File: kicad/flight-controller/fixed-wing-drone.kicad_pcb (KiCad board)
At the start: 4 copper layers, 91 x 61.5 mm, 81 parts, among them J1 1, J10 UWB SPI, J11 Inter ESP UART, J13 USB-C, J14 GPS/Compass, J15 Airspeed I2C, J16 8, J19 ESC2, J2 2, J20 FC UBEC Input, J22 ESC1, J3 3, J4 4, J5 5, J6 6, J7 RC Conn, J8 LIDAR I2C, J9 7, M2 MountingHole_2.2mm_M2, Q1 reverse polarity protection, Q2 reverse polarity protection, SW1 TS-1088, SW2 TS-1088, U1 ESP32-S3-WROOM-1, U2 Primary IMU, U3 Backup IMU, U4 XC6220B331PR-G, U6 AP2112K-3.3, U7 Barometer

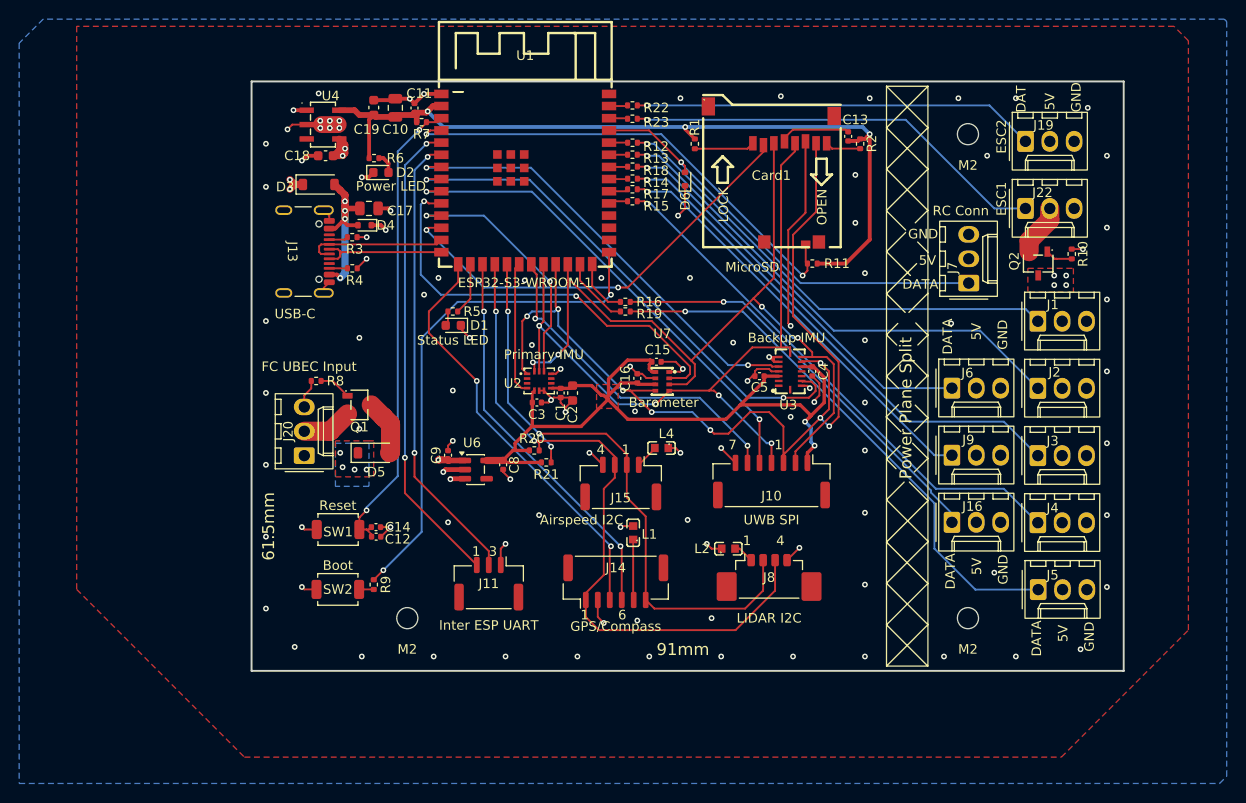
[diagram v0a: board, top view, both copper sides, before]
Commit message: removed basestation code and v3.1 of fc pcb
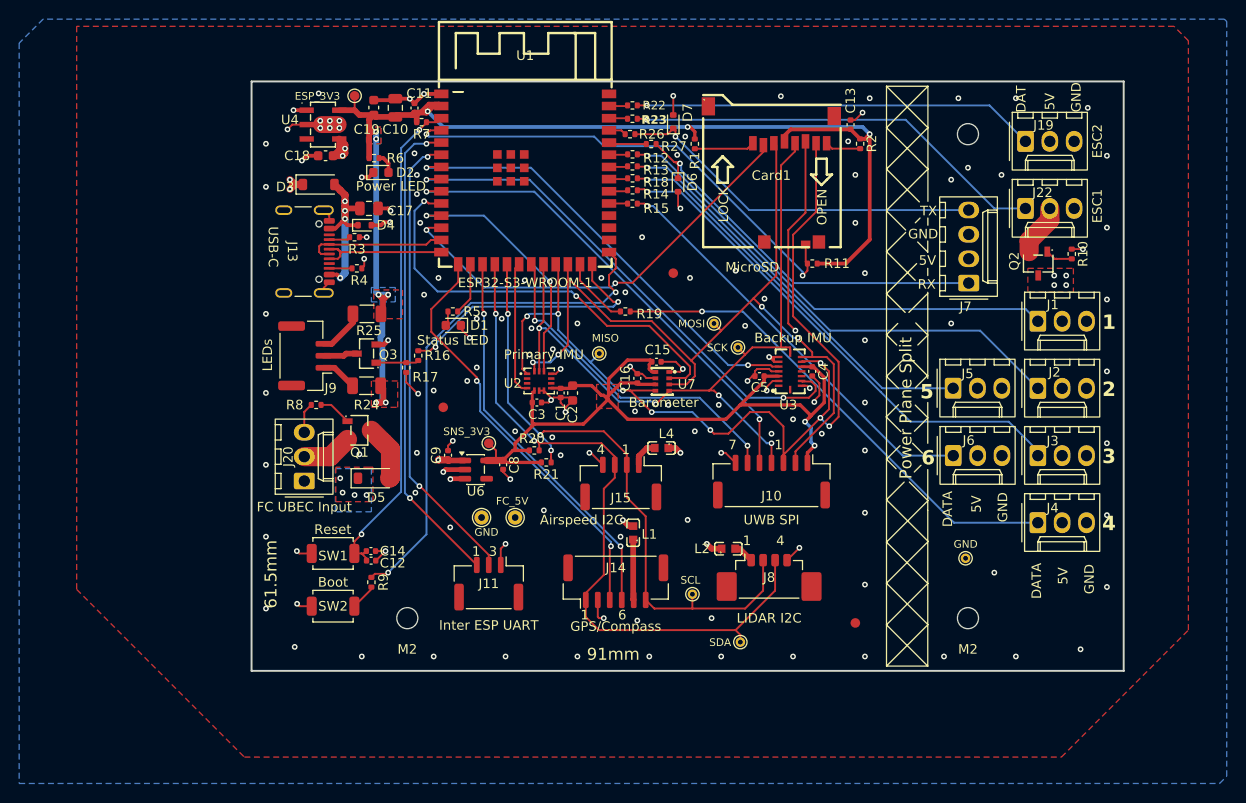
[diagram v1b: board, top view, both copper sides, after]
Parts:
- removed J16: 8, Connector_Molex:Molex_KK-254_AE-6410-03A_1x03_P2.54mm_Vertical
- added D7: ESD5Z5.0T1G, Diode_SMD:D_SOD-523, F.Cu at (142.2, 66.5)
- added Q3: AO3400A, easyeda2kicad:SOT-23-3_L2.9-W1.3-P1.90-LS2.4-BR, F.Cu at (110.2, 90.6)
- added R24: 33R, Resistor_SMD:R_1206_3216Metric, F.Cu at (110.2, 94.0)
- added R25: 33R, Resistor_SMD:R_1206_3216Metric, F.Cu at (110.3, 86.5)
- added R26: 330R, Resistor_SMD:R_0402_1005Metric, F.Cu at (137.7, 67.8)
- added R27: 330R, Resistor_SMD:R_0402_1005Metric, F.Cu at (139.9, 68.8)
- added REF**: Fiducial_1mm_Mask2mm, Fiducial:Fiducial_1mm_Mask2mm, F.Cu at (161.2, 118.8)
- added REF**: Fiducial_1mm_Mask2mm, Fiducial:Fiducial_1mm_Mask2mm, F.Cu at (142.2, 82.2)
- added REF**: Fiducial_1mm_Mask2mm, Fiducial:Fiducial_1mm_Mask2mm, F.Cu at (118.2, 96.2)
- added TP1: MOSI, TestPoint:TestPoint_THTPad_D1.0mm_Drill0.5mm, F.Cu at (146.5, 87.5)
- added TP10: GND, TestPoint:TestPoint_THTPad_D1.0mm_Drill0.5mm, F.Cu at (172.8, 112.0)
- added TP2: MISO, TestPoint:TestPoint_THTPad_D1.0mm_Drill0.5mm, F.Cu at (134.5, 90.6)
- added TP3: SCK, TestPoint:TestPoint_THTPad_D1.0mm_Drill0.5mm, F.Cu at (149.0, 90.0)
- added TP4: GND, TestPoint:TestPoint_THTPad_D1.5mm_Drill0.7mm, F.Cu at (122.2, 107.8)
- added TP5: SDA, TestPoint:TestPoint_THTPad_D1.0mm_Drill0.5mm, F.Cu at (149.2, 120.8)
- added TP6: SCL, TestPoint:TestPoint_THTPad_D1.0mm_Drill0.5mm, F.Cu at (144.2, 115.8)
- added TP7: ESP_3V3, TestPoint:TestPoint_Pad_D1.0mm, F.Cu at (109.0, 63.8)
- added TP8: SENSOR_3V3, TestPoint:TestPoint_Pad_D1.0mm, F.Cu at (123.0, 100.0)
- added TP9: FC_5V, TestPoint:TestPoint_THTPad_D1.5mm_Drill0.7mm, F.Cu at (125.8, 107.8)
- J7: footprint Connector_Molex:Molex_KK-254_AE-6410-03A_1x03_P2.54mm_Vertical -> Connector_Molex:Molex_KK-254_AE-6410-04A_1x04_P2.54mm_Vertical
- J9: value 7 -> Conn_01x03_Pin; footprint Connector_Molex:Molex_KK-254_AE-6410-03A_1x03_P2.54mm_Vertical -> Connector_JST:JST_GH_BM03B-GHS-TBT_1x03-1MP_P1.25mm_Vertical
- R16: value 330R -> 220R
- R17: value 330R -> 100K
- moved J9 68.3 mm to (103.8, 90.9), turned to 90 degrees
- moved R17 30.0 mm to (114.4, 92.1), turned to -90 degrees
- moved J5 22.8 mm to (171.5, 94.3)
- moved R16 22.3 mm to (115.6, 90.9), turned to -90 degrees
- moved J6 7.04 mm to (171.5, 101.3)
- moved D5 2.65 mm to (111.0, 103.7)
- moved Q1 2.65 mm to (109.5, 98.7)
- moved J20 2.65 mm to (103.8, 103.9)
- moved C12 2.55 mm to (110.7, 112.2)
- moved C14 2.55 mm to (110.7, 111.2)
- moved SW1 2.55 mm to (106.8, 111.5)
- moved R8 2.50 mm to (105.0, 96.0)
- moved SW2 1.82 mm to (106.8, 117.0)
- moved C13 1.26 mm to (160.8, 66.8), turned to -90 degrees
- moved R12 1.21 mm to (138.0, 69.9)
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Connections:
- net /SERVO_OUT4 renamed /SERVO_OUT_6
- net /SERVO_OUT5 renamed /SERVO_OUT_4
- net /SERVO_OUT8 renamed /LED_TOGGLE
- C13 pad 1: /ESP_3V3 -> GND
- C13 pad 2: Net-(Card1-VDD) -> /ESP_3V3
- Card1 pad 4: Net-(Card1-VDD) -> /ESP_3V3
- D4 pad 1: GND -> Net-(D3-A)
- D4 pad 2: Net-(D3-A) -> GND
- D6 pad 1: GND -> /actuator_io/RC_SBUS_TVS
- D6 pad 2: /RC_SBUS -> GND
- J7 pad 1: /RC_SBUS -> /actuator_io/RC_SBUS_TVS
- J9 pad 1: Net-(J9-Pin_1) -> /aux/IRLED_FEED_1
- J9 pad 2: /actuator_io/esc_io/SERVO_5V -> /aux/IRLED_SW
- J9 pad 3: GND -> /aux/IRLED_FEED_2
- R12 pad 1: /SERVO_OUT1 -> /SERVO_OUT_1
- R13 pad 1: /SERVO_OUT2 -> /SERVO_OUT_2
- R14 pad 1: /SERVO_OUT3 -> /SERVO_OUT_3
- R15 pad 2: Net-(J4-Pin_1) -> Net-(J6-Pin_1)
- R16 pad 2: Net-(J16-Pin_1) -> Net-(Q3-G)
- R17 pad 1: /SERVO_OUT7 -> Net-(Q3-G)
- R17 pad 2: Net-(J9-Pin_1) -> GND
- R18 pad 1: /SERVO_OUT6 -> /SERVO_OUT_5
- R18 pad 2: Net-(J6-Pin_1) -> Net-(J5-Pin_1)
- R19 pad 2: Net-(J5-Pin_1) -> Net-(J4-Pin_1)
- U1 pad 32: /SERVO_OUT7 -> /SERVO_OUT_3
- U1 pad 33: /SERVO_OUT3 -> /SERVO_OUT_5
- U1 pad 34: /SERVO_OUT6 -> /SERVO_OUT_2
- U1 pad 35: /SERVO_OUT2 -> /SERVO_OUT_1
- U1 pad 36: /SERVO_OUT1 -> /RC_SBUS
- U1 pad 37: /RC_SBUS -> /RC_TX
- U3 pad 2: unconnected-(U3-NC-Pad2) -> GND
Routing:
- net /ESP_3V3: track 86.2 -> 136.2 mm, vias 3 -> 9
- net Net-(J9-Pin_1): track 44.3 -> 0.00 mm, vias 1 -> 0
- net Net-(J16-Pin_1): track 43.9 -> 0.00 mm, vias 1 -> 0
- net /RC_SBUS: track 45.5 -> 3.95 mm, vias 1 -> 0
- net /actuator_io/RC_SBUS_TVS: track 0.00 -> 40.7 mm, vias 0 -> 1
- net Net-(D7-A1): track 0.00 -> 39.0 mm, vias 0 -> 1
- net /LED_TOGGLE: track 5.93 -> 28.6 mm, vias 0 -> 2
- net Net-(J5-Pin_1): track 57.4 -> 42.0 mm
- net GND: track 102.2 -> 110.5 mm, vias 99 -> 133
- net Net-(Card1-VDD): track 7.44 -> 0.00 mm
- net /aux/IRLED_FEED_2: track 0.00 -> 4.89 mm
- net Net-(Q3-G): track 0.00 -> 4.17 mm
- net Net-(J4-Pin_1): track 55.7 -> 51.7 mm
- net /aux/IRLED_FEED_1: track 0.00 -> 3.79 mm
- net /aux/IRLED_SW: track 0.00 -> 3.57 mm
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- added copper zone on B.Cu, net /ESP_3V3
- added copper zone on F.Cu, net /ESP_3V3
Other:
- board text added: "1"
- board text added: "2"
- board text added: "3"
- board text added: "4"
- board text added: "5"
- board text added: "6"
- board text added: "ESP_3V3"
- board text added: "FC_5V"
- board text added: "LEDs"
- board text added: "MISO"
- board text added: "MOSI"
- board text added: "RX"
- board text added: "SCK"
- board text added: "SCL"
- board text added: "SDA"
- board text added: "SNS_3V3"
- board text added: "TX"

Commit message: pcb progress
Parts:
- added D8: ESD5Z5.0T1G, Diode_SMD:D_SOD-523, F.Cu at (112.8, 81.5)
- added D9: ESD5Z5.0T1G, Diode_SMD:D_SOD-523, F.Cu at (113.5, 78.5)
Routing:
- net GND: track 110.5 -> 114.1 mm, vias 133 -> 136
- net /esp32s3/DATA-: track 14.8 -> 15.6 mm
- net /esp32s3/DATA+: track 14.9 -> 15.6 mm

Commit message: Kicad FC v3.1 complete, Mission Controller and UWB boards v1 complete, firmware v2 complete!
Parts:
- removed D8, D9: ESD5Z5.0T1G, Diode_SMD:D_SOD-523
- removed Q1, Q2: reverse polarity protection, easyeda2kicad:SOT-23-3_L2.9-W1.6-P1.90-LS2.8-BR
- removed R10, R8: 100K, Resistor_SMD:R_0402_1005Metric
- added C20: 22uF, Capacitor_SMD:C_0805_2012Metric, F.Cu at (178.1, 81.8)
- added L3: Ferrite Bead, easyeda2kicad:L0603, F.Cu at (159.4, 99.7)
- added R28: 10K, Resistor_SMD:R_0402_1005Metric, F.Cu at (153.3, 81.2)
- added R29: 10K, Resistor_SMD:R_0402_1005Metric, F.Cu at (153.3, 83.7)
- added R30: 10K, Resistor_SMD:R_0402_1005Metric, F.Cu at (153.3, 82.5)
- added U5: USBLC6-2SC6, Package_TO_SOT_SMD:SOT-23-6, F.Cu at (113.4, 79.8)
- C18: value 10uF -> 22uF; footprint Capacitor_SMD:C_0603_1608Metric -> Capacitor_SMD:C_0805_2012Metric
- R20, R21: value 6.8K -> 4.7K
- moved C12 44.8 mm to (113.9, 67.6), turned to 180 degrees
- moved C14 42.8 mm to (113.9, 68.6), turned to 180 degrees
- moved D6 28.6 mm to (168.6, 85.4)
- moved D7 27.5 mm to (168.8, 73.8)
- moved D5 2.30 mm to (109.4, 102.0), turned to 90 degrees
- moved J13 0.81 mm to (101.9, 80.0)
- moved C18 0.55 mm to (105.6, 70.4)
- moved R11 0.51 mm to (156.2, 81.3), turned to 90 degrees
- moved TP1 0.25 mm to (146.5, 87.8)
- renumbered REF** to FID1, REF** to FID2, REF** to FID3, M2 to H1, M2 to H2, M2 to H3
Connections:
- net Net-(D3-A) renamed /esp32s3/USB_VBUS
- Card1 pad 3: /MOSI -> /SD_MOSI
- Card1 pad 5: /SCK -> /SD_SCK
- Card1 pad 7: /MISO -> /SD_MISO
- J10 pad 1: /SENSOR_3V3 -> Net-(J10-Pin_1)
- J20 pad 1: unconnected-(J20-Pin_1-Pad1) -> GND
- J20 pad 2: Net-(J20-Pin_2) -> Net-(D5-A)
- J22 pad 2: Net-(J22-Pin_2) -> /actuator_io/esc_io/SERVO_5V
- U1 pad 12: /SD_CS -> /SD_MISO
- U1 pad 28: unconnected-(U1-IO35-Pad28) -> /SD_SCK
- U1 pad 29: unconnected-(U1-IO36-Pad29) -> /SD_MOSI
- U1 pad 30: unconnected-(U1-IO37-Pad30) -> /SD_CS
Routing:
- net /SD_MISO: track 0.00 -> 57.7 mm, vias 0 -> 2
- net /SD_MOSI: track 0.00 -> 35.6 mm, vias 0 -> 2
- net /MISO: track 107.3 -> 73.1 mm, vias 9 -> 7
- net /SD_SCK: track 0.00 -> 23.8 mm
- net /SCK: track 77.7 -> 55.8 mm
- net /MOSI: track 87.3 -> 67.5 mm, vias 4 -> 2
- net /actuator_io/esc_io/SERVO_5V: track 0.00 -> 15.1 mm, vias 4 -> 9
- net /SD_CS: track 45.8 -> 38.5 mm
- net /SENSOR_3V3: track 90.4 -> 83.6 mm, vias 2 -> 0
- net /ESP_3V3: track 136.0 -> 142.5 mm
- net /esp32s3/USB_VBUS: track 19.1 -> 25.2 mm, vias 4 -> 5
- net Net-(J22-Pin_2): track 5.40 -> 0.00 mm
- net Net-(J20-Pin_2): track 5.26 -> 0.00 mm
- net /FC_5V: track 18.5 -> 22.6 mm, vias 14 -> 15
- net Net-(J10-Pin_1): track 0.00 -> 4.03 mm
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- removed copper zone on B.Cu, net /FC_5V
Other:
- board text added: "3 1"
- board text added: "Autonomous Fixed Wing Flight Controller v3.1"
- board text added: "Din"
- board text added: "Dout"
- board text added: "October 2026"
- board text removed: "1 3"
- board text removed: "Autonomous Fixed Wing Flight Controller v3.0"
- board text removed: "RX"
- board text removed: "September 2026"
- board text removed: "TX"
